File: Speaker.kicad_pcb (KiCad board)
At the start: 2 copper layers, 55.8 x 60 mm, 93 parts, among them J2 UJ20-C-H-G-SMT-1-P16-TR, SW1 SW_Push, SW2 Volume Up, SW3 Volume Down, SW4 Play/Pause, SW5 Power Switch, U2 MCP73871, U3 AP2112K-3.3, U4 MAX17048G_T10, U5 USBLC6-2SC6, U6 CH340X, U7 ESP32-WROOM-32, U8 MAX98357A, U9 USBLC6-2SC6

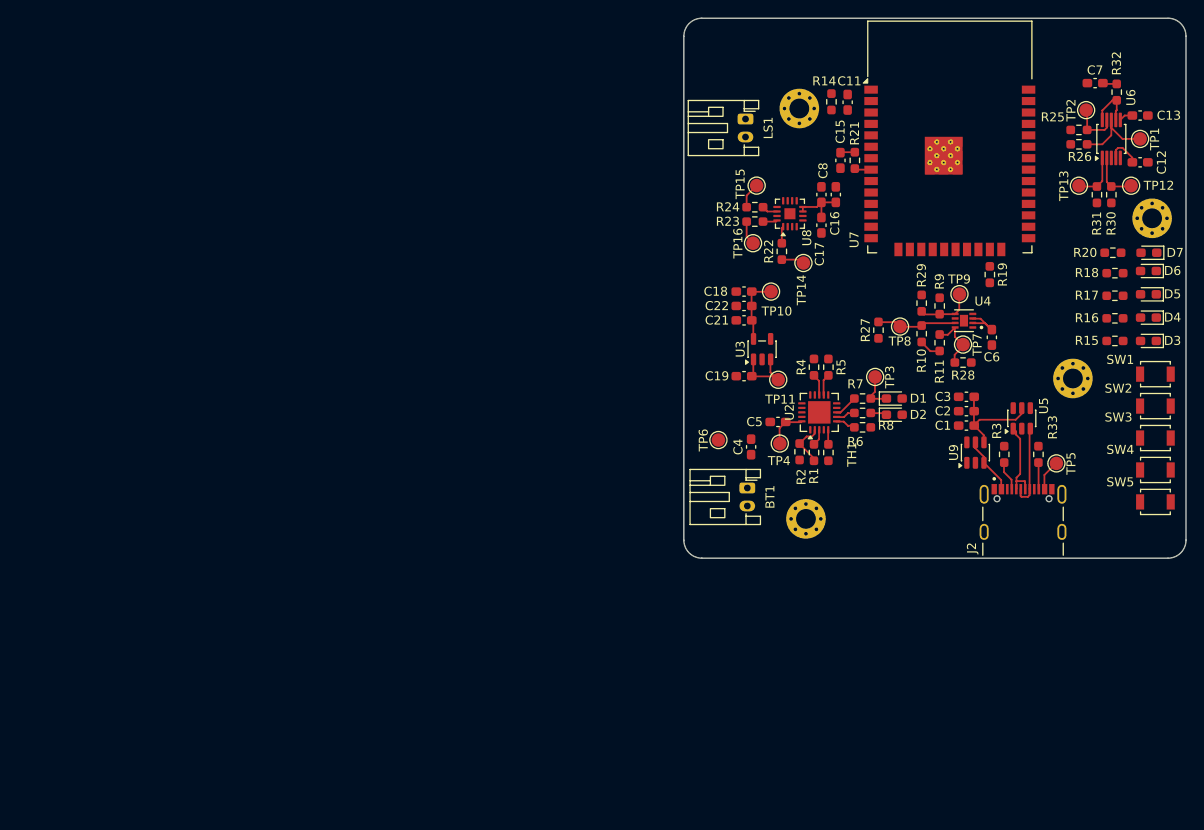
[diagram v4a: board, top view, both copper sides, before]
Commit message: Add 3d models and design rules
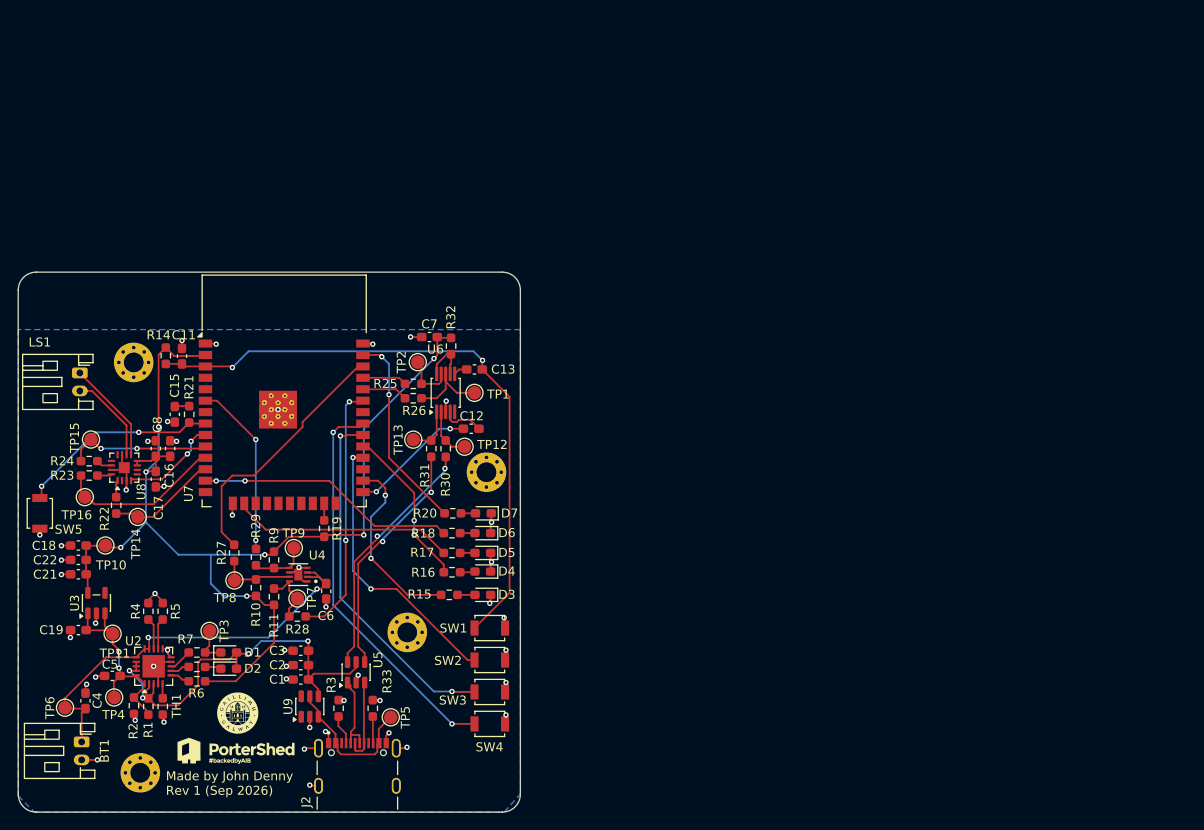
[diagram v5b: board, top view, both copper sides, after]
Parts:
- added G***: LOGO, LOGO, F.Cu at (157.0, 115.8)
- added G***: LOGO, LOGO, F.Cu at (157.2, 111.6)
- moved SW5 124.0 mm to (135.2, 89.4), turned to -90 degrees
- moved C12 80.0 mm to (183.2, 80.0), turned to 0 degrees
- moved TP12 79.5 mm to (182.4, 82.0)
- moved D6 79.5 mm to (184.5, 91.6)
- moved TP16 79.4 mm to (140.2, 87.6)
- moved D7 79.4 mm to (184.5, 89.4)
- moved TP2 79.4 mm to (177.2, 72.6)
- moved D5 79.4 mm to (184.5, 93.8)
- moved C18 79.2 mm to (139.5, 93.0)
- moved C19 79.2 mm to (139.5, 102.4)
- moved C21 79.2 mm to (139.5, 96.2)
- moved C22 79.2 mm to (139.5, 94.6)
- moved D3 79.2 mm to (184.5, 98.5)
- moved D4 79.2 mm to (184.5, 95.9)
- moved H4 79.2 mm to (184.9, 84.8)
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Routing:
- net VREG_3.3V: track 17.5 -> 124.0 mm, vias 0 -> 7
- net Net-(U7-EN): track 0.00 -> 69.2 mm, vias 0 -> 2
- net GND: track 0.00 -> 63.8 mm, vias 0 -> 47
- net Net-(U7-IO19): track 0.00 -> 44.1 mm, vias 0 -> 2
- net VBAT+: track 5.04 -> 47.5 mm, vias 0 -> 2
- net Net-(U7-IO18): track 0.00 -> 39.8 mm, vias 0 -> 2
- net VDD: track 13.8 -> 45.4 mm, vias 0 -> 4
- net Net-(U7-IO17): track 0.00 -> 31.3 mm, vias 0 -> 2
- net Net-(U7-IO14): track 0.00 -> 28.9 mm, vias 0 -> 2
- net FuelGaugeSDA: track 0.00 -> 28.6 mm, vias 0 -> 2
- net FuelGaugeSCL: track 0.00 -> 28.6 mm
- net D-: track 0.00 -> 27.5 mm, vias 0 -> 2
- net D+: track 0.00 -> 26.8 mm, vias 0 -> 2
- net Net-(U7-IO13): track 0.00 -> 24.8 mm
- net Net-(U7-IO23): track 0.00 -> 22.5 mm, vias 0 -> 2
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- added copper zone on B.Cu, net GND

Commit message: Update speaker PCB design
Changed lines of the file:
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@@
 		(start 140.308274 111.116726)
 		(end 138.133274 111.116726)
-		(width 0.2)
+		(width 0.4)
 		(layer "F.Cu")
 		(net 2)
@@
 		(start 138.033274 109.966783)
 		(end 138.033274 111.016726)
-		(width 0.2)
+		(width 0.4)
 		(layer "F.Cu")
 		(net 2)
@@
 		(start 139.883274 114.816726)
 		(end 139.883274 111.541726)
-		(width 0.2)
+		(width 0.4)
 		(layer "F.Cu")
 		(net 2)
@@
 		(start 145.945774 105.416726)
 		(end 142.583331 105.416726)
-		(width 0.2)
+		(width 0.4)
 		(layer "F.Cu")
 		(net 2)
@@
 		(start 142.583331 105.416726)
 		(end 138.033274 109.966783)
-		(width 0.2)
+		(width 0.4)
 		(layer "F.Cu")
 		(net 2)
@@
 		(start 146.883274 104.479226)
 		(end 145.945774 105.416726)
-		(width 0.2)
+		(width 0.4)
 		(layer "F.Cu")
 		(net 2)
@@
 		(start 146.883274 108.354226)
 		(end 145.945774 107.416726)
-		(width 0.2)
+		(width 0.4)
 		(layer "F.Cu")
 		(net 3)
@@
 		(start 143.468274 109.904226)
 		(end 143.468274 108.166726)
-		(width 0.2)
+		(width 0.4)
 		(layer "F.Cu")
 		(net 3)
@@
 		(start 143.468274 108.166726)
 		(end 144.130774 107.504226)
-		(width 0.2)
+		(width 0.4)
 		(layer "F.Cu")
 		(net 3)
@@
 		(start 145.820774 107.541726)
 		(end 144.218274 107.541726)
-		(width 0.2)
-		(layer "F.Cu")
-		(net 3)
+		(width 0.4)
+		(layer "F.Cu")
+		(net 3)

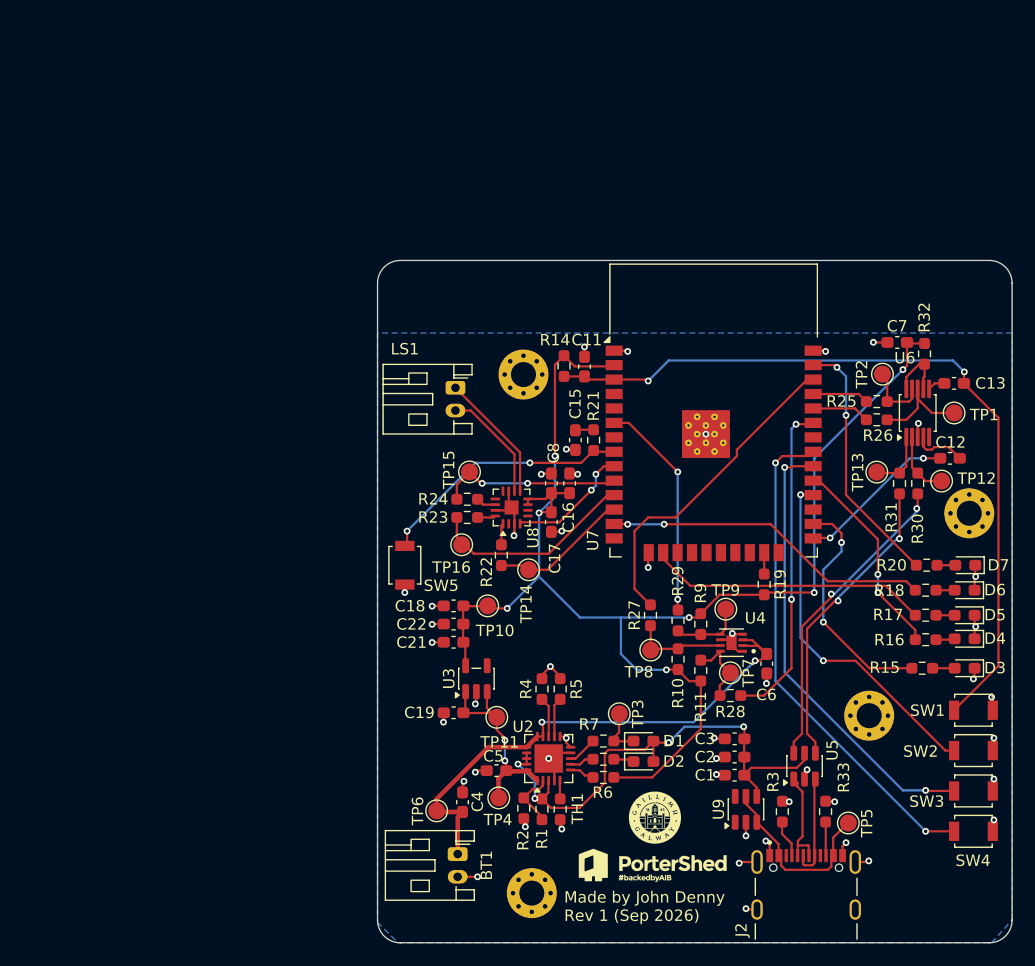
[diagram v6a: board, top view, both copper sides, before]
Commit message: Mostly finished schematic and pcb, getting codex to review it now
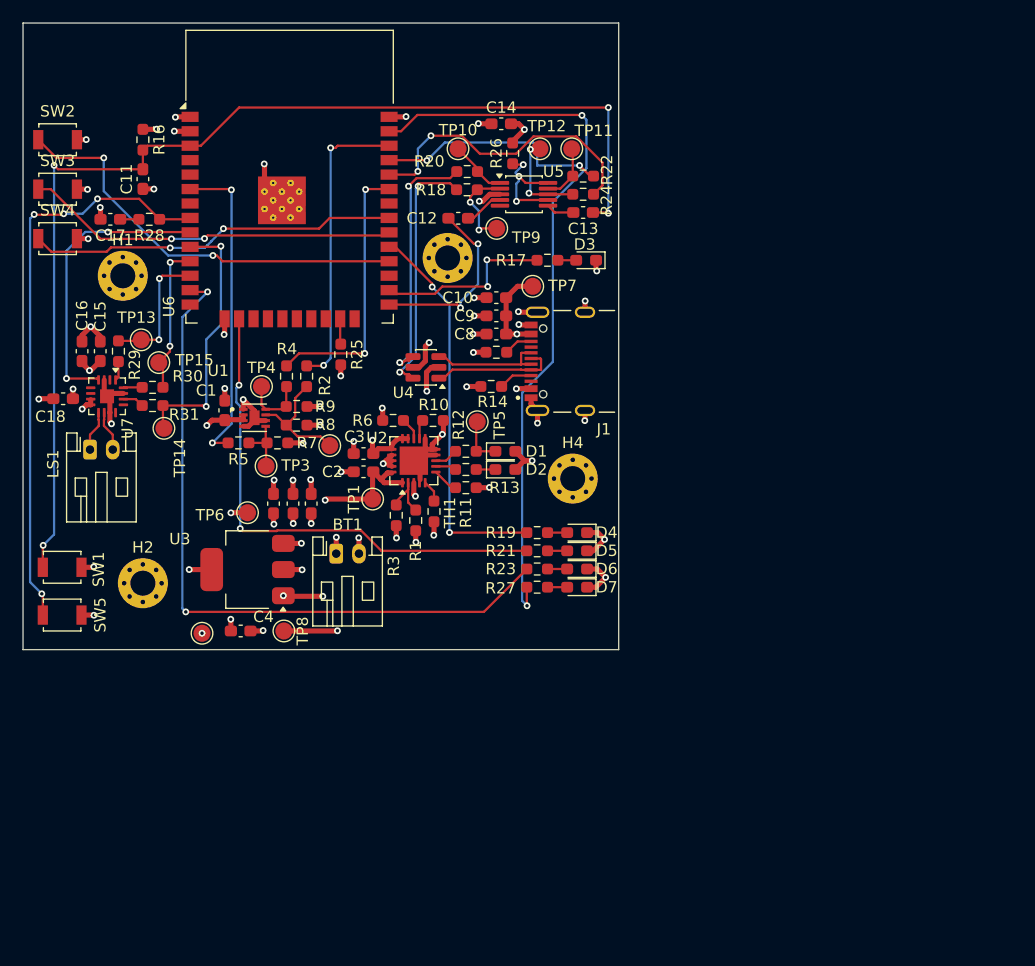
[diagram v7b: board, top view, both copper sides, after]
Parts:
- removed C19: 1uF, Capacitor_SMD:C_0603_1608Metric_Pad1.08x0.95mm_HandSolder
- removed C21: 100pF, Capacitor_SMD:C_0603_1608Metric_Pad1.08x0.95mm_HandSolder
- removed C22: 100nF, Capacitor_SMD:C_0603_1608Metric_Pad1.08x0.95mm_HandSolder
- removed G*** (x2): LOGO, LOGO
- removed H5, H6: MountingHole, MountingHole:MountingHole_2.2mm_M2_Pad_Via
- removed J2: UJ20-C-H-G-SMT-1-P16-TR, UJ20-C-H-G-SMT-1-P16-TR:SAMESKY_UJ20-C-H-G-SMT-1-P16-TR
- removed R32: 0, Resistor_SMD:R_0603_1608Metric_Pad0.98x0.95mm_HandSolder
- removed R33: 5.1k, Resistor_SMD:R_0603_1608Metric_Pad0.98x0.95mm_HandSolder
- removed TP16: TP_BCLK, TestPoint:TestPoint_Pad_D1.5mm
- removed U8: MAX98357A, Package_DFN_QFN:TQFN-16-1EP_3x3mm_P0.5mm_EP1.23x1.23mm
- removed U9: USBLC6-2SC6, Package_TO_SOT_SMD:SOT-23-6
- added C10: 1uF, Capacitor_SMD:C_0603_1608Metric_Pad1.08x0.95mm_HandSolder, F.Cu at (143.3, 65.9)
- added C14: 0.1uF, Capacitor_SMD:C_0603_1608Metric_Pad1.08x0.95mm_HandSolder, F.Cu at (143.7, 50.6)
- added C9: 100pF, Capacitor_SMD:C_0603_1608Metric_Pad1.08x0.95mm_HandSolder, F.Cu at (143.3, 67.5)
- added H1: MountingHole, MountingHole:MountingHole_2.2mm_M2_Pad_Via, F.Cu at (110.4, 64.0)
- added H2: MountingHole, MountingHole:MountingHole_2.2mm_M2_Pad_Via, F.Cu at (112.2, 91.0)
- added J1: UJ20-C-H-G-SMT-1-P16-TR, UJ20-C-H-G-SMT-1-P16-TR:SAMESKY_UJ20-C-H-G-SMT-1-P16-TR, F.Cu at (153.7, 71.5)
- added R12: ~, Resistor_SMD:R_0603_1608Metric_Pad0.98x0.95mm_HandSolder, F.Cu at (140.6, 79.4)
- added R13: ~, Resistor_SMD:R_0603_1608Metric_Pad0.98x0.95mm_HandSolder, F.Cu at (140.6, 81.0)
- added TP_VSYS_LDO1: TP_VSYS_LDO, TestPoint:TestPoint_Pad_D1.5mm, F.Cu at (117.4, 95.4)
- added U1: MAX17048G_T10, MAX17048G_T10:SON50P200X200X80-9N, F.Cu at (122.0, 76.5)
- C1: value 1uF -> 0.1uF
- C15: value 100nF -> 10uF
- C16: value 10uF -> 100nF
- C18: value 1uF -> 1nF
- C2: value 100pF -> 4.7uF
- C3: value 100nF -> 4.7uF
- C4: value 4.7uF -> 1uF
- C5: value 4.7uF -> 100nF
- C6: value 0.1uF -> 100pF
- C7: value 0.1uF -> 1uF
- C8: value 1nF -> 100nF
- R10: value 4.7k -> 10k
- R11: value 4.7k -> 470
- R14: value 10k -> 5.1k
- R15: value R -> 5.1k
- R16: value R -> 10k
- R18, R20: value R -> 0
- R19, R21: value 10k -> R
- R2: value 110k -> 0
- R23, R27: value 0 -> R
- R25, R28: value 0 -> 10k
- R3: value 5.1k -> 110k
- R4: value 1k -> 0
- R5: value 10k -> 0
- R6: value 470 -> 1k
- R7, R8: value ~ -> 4.7k
- TP1: value TP_UART_TX -> TP_VSYS
- TP10: value TP_VREG3.3 -> TP_D+
- TP11: value TP_VSYS_LDO -> TP_UART_RX
- TP12: value TP_D- -> TP_UART_TX
- TP13: value TP_D+ -> TP_DIN
- TP15: value TP_DIN -> TP_BCLK
- TP2: value TP_UART_RX -> TP_FG_SCL
- TP3: value TP_Charging -> TP_FG_ALRT
- TP4: value TP_VSYS -> TP_FG_SDA
- TP5: value TP_VDD -> TP_Charging
- TP6: value TP_VBAT+ -> TP_VREG3.3
- TP7: value TP_FG_SDA -> TP_VDD
- TP8: value TP_FG_SCL -> TP_VBAT+
- TP9: value TP_FG_ALRT -> TP_D-
- U3: value AP2112K-3.3 -> LT1963AxST-3.3; footprint Package_TO_SOT_SMD:SOT-23-5 -> Package_TO_SOT_SMD:SOT-223-3_TabPin2
- U4: value MAX17048G_T10 -> USBLC6-2SC6; footprint MAX17048G_T10:SON50P200X200X80-9N -> Package_TO_SOT_SMD:SOT-23-6
- U5: value USBLC6-2SC6 -> CH340X; footprint Package_TO_SOT_SMD:SOT-23-6 -> Package_SO:MSOP-10_3x3mm_P0.5mm
- U6: value CH340X -> ESP32-WROOM-32; footprint Package_SO:MSOP-10_3x3mm_P0.5mm -> RF_Module:ESP32-WROOM-32
- U7: value ESP32-WROOM-32 -> MAX98357A; footprint RF_Module:ESP32-WROOM-32 -> Package_DFN_QFN:TQFN-16-1EP_3x3mm_P0.5mm_EP1.23x1.23mm
- moved SW2 96.8 mm to (104.7, 52.0)
- moved SW3 96.4 mm to (104.7, 56.4)
- moved SW4 95.9 mm to (104.7, 60.7)
- moved R16 81.7 mm to (112.2, 52.0), turned to -90 degrees
- moved SW1 81.1 mm to (105.1, 89.6)
- moved R30 67.8 mm to (113.0, 73.8), turned to 180 degrees
- moved R28 66.1 mm to (112.8, 59.0)
- moved R31 66.0 mm to (113.0, 75.4), turned to 180 degrees
- moved TP13 65.7 mm to (112.0, 69.6), turned to -90 degrees
- moved U6 58.0 mm to (125.1, 58.2), turned to 0 degrees
- moved C7 56.6 mm to (123.7, 84.0), turned to -90 degrees
- moved U5 56.0 mm to (145.7, 56.8), turned to 0 degrees
- moved C1 55.1 mm to (119.4, 75.8), turned to 90 degrees
- moved H3 54.7 mm to (139.0, 62.4)
- moved R29 54.6 mm to (110.0, 70.6), turned to -90 degrees
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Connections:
- C1 pad 1: GND -> VBAT+
- C1 pad 2: VDD -> GND
- C11 pad 2: Net-(U7-EN) -> Enable
- C12 pad 1: Net-(U7-IO0) -> Net-(U6-IO0)
- C12 pad 2: Net-(U6-~{RTS}) -> Net-(U5-~{RTS})
- C13 pad 1: Net-(U7-EN) -> Enable
- C13 pad 2: Net-(U6-TNOW/~{DTR}) -> Net-(U5-TNOW/~{DTR})
- C15 pad 1: Net-(C15-Pad1) -> GND
- C15 pad 2: GND -> VREG_3.3V
- C17 pad 1: GND -> Net-(C17-Pad1)
- C17 pad 2: VREG_3.3V -> GND
- C2 pad 1: GND -> VSYS
- C2 pad 2: VDD -> GND
- C3 pad 1: GND -> VBAT+
- C3 pad 2: VDD -> GND
- C4 pad 1: VBAT+ -> GND
- C4 pad 2: GND -> VSYS
- C5 pad 1: VSYS -> GND
- C5 pad 2: GND -> VREG_3.3V
- C6 pad 1: VBAT+ -> GND
- C6 pad 2: GND -> VREG_3.3V
- C8 pad 2: VREG_3.3V -> VDD
- LS1 pad 1: Net-(U8-OUTP) -> /MCU/Speaker+
- LS1 pad 2: Net-(U8-OUTN) -> /MCU/Speaker-
- R10 pad 1: Net-(U4-SCL) -> GND
- R10 pad 2: VREG_3.3V -> Net-(U2-PROG3)
- R11 pad 1: Net-(U4-SDA) -> Net-(U2-~{PG})
- R14 pad 1: VREG_3.3V -> GND
- R14 pad 2: Net-(U7-EN) -> Net-(J1-CC1)
- R15 pad 1: Net-(U7-IO4) -> Net-(J1-CC2)
- R15 pad 2: Net-(D3-A) -> GND
- R16 pad 1: Net-(U7-IO5) -> VREG_3.3V
- R16 pad 2: Net-(D4-A) -> Enable
- R17 pad 1: Net-(U7-IO13) -> Net-(U6-IO4)
- R17 pad 2: Net-(D5-A) -> Net-(D3-A)
- R18 pad 1: Net-(U7-IO14) -> Net-(U5-UD-)
- R18 pad 2: Net-(D6-A) -> D-
- R19 pad 1: Net-(U7-IO15) -> Net-(U6-IO5)
- R19 pad 2: VREG_3.3V -> Net-(D4-A)
- R2 pad 1: GND -> FuelGaugeSCL
- R2 pad 2: Net-(U2-VPCC) -> Net-(U1-SCL)
- R20 pad 1: Net-(U7-IO23) -> Net-(U5-UD+)
- R20 pad 2: Net-(D7-A) -> D+
- R21 pad 1: Net-(U7-IO32) -> Net-(U6-IO13)
- R21 pad 2: Net-(C15-Pad1) -> Net-(D5-A)
- R22 pad 1: /MCU/AMP_DIN -> /MCU/RX_UART
- R22 pad 2: Net-(U8-DIN) -> Net-(U5-RXD)
- R23 pad 1: /MCU/AMP_BCLK -> Net-(U6-IO14)
- R23 pad 2: Net-(U8-BCLK) -> Net-(D6-A)
- R24 pad 1: /MCU/AMP_LRCLK -> /MCU/TX_UART
- R24 pad 2: Net-(U8-LRCLK) -> Net-(U5-TXD)
- R25 pad 1: /MCU/RX_UART -> Net-(U6-IO15)
- R25 pad 2: Net-(U6-RXD) -> VREG_3.3V
- R26 pad 1: /MCU/TX_UART -> Net-(U5-V3)
- R26 pad 2: Net-(U6-TXD) -> VREG_3.3V
- R27 pad 1: FuelGaugeSCL -> Net-(U6-IO23)
- R27 pad 2: Net-(U4-SCL) -> Net-(D7-A)
- R28 pad 1: FuelGaugeSDA -> Net-(U6-IO32)
- R28 pad 2: Net-(U4-SDA) -> Net-(C17-Pad1)
- R29 pad 1: Net-(U4-~{ALERT}) -> /MCU/AMP_DIN
- R29 pad 2: FuelGaugeAlert -> Net-(U7-DIN)
- R3 pad 2: Net-(J2-CC1) -> Net-(U2-VPCC)
- R30 pad 1: Net-(U6-UD-) -> /MCU/AMP_BCLK
- R30 pad 2: D- -> Net-(U7-BCLK)
- R31 pad 1: Net-(U6-UD+) -> /MCU/AMP_LRCLK
- R31 pad 2: D+ -> Net-(U7-LRCLK)
- R4 pad 1: GND -> FuelGaugeSDA
- R4 pad 2: Net-(U2-PROG1) -> Net-(U1-SDA)
- R5 pad 1: GND -> Net-(U1-~{ALERT})
- R5 pad 2: Net-(U2-PROG3) -> FuelGaugeAlert
- R6 pad 1: Net-(U2-~{PG}) -> GND
- R6 pad 2: VREG_3.3V -> Net-(U2-PROG1)
- R7 pad 1: Net-(U2-STAT1/~{LBO}) -> Net-(U1-~{ALERT})
- R7 pad 2: Net-(D1-K) -> VREG_3.3V
- R8 pad 1: Net-(U2-STAT2) -> Net-(U1-SCL)
- R8 pad 2: Net-(D2-K) -> VREG_3.3V
- R9 pad 1: Net-(U4-~{ALERT}) -> Net-(U1-SDA)
- SW1 pad 2: Net-(U7-EN) -> Enable
- SW2 pad 1: Net-(U7-IO17) -> Net-(U6-IO17)
- SW3 pad 1: Net-(U7-IO18) -> Net-(U6-IO18)
- SW4 pad 1: Net-(U7-IO19) -> Net-(U6-IO19)
- SW5 pad 1: Net-(U7-IO32) -> Net-(U6-IO32)
- TP1 pad 1: Net-(U6-TXD) -> VSYS
- TP10 pad 1: VREG_3.3V -> Net-(U5-UD+)
- TP11 pad 1: VSYS -> Net-(U5-RXD)
- TP12 pad 1: Net-(U6-UD-) -> Net-(U5-TXD)
- TP13 pad 1: Net-(U6-UD+) -> /MCU/AMP_DIN
- TP14 pad 1: /MCU/AMP_DIN -> /MCU/AMP_LRCLK
- TP15 pad 1: /MCU/AMP_LRCLK -> /MCU/AMP_BCLK
- TP2 pad 1: Net-(U6-RXD) -> Net-(U1-SCL)
- TP3 pad 1: Net-(D1-K) -> Net-(U1-~{ALERT})
- TP4 pad 1: VSYS -> Net-(U1-SDA)
- TP5 pad 1: Net-(U9-VBUS) -> Net-(D1-K)
- TP6 pad 1: VBAT+ -> VREG_3.3V
- TP7 pad 1: Net-(U4-SDA) -> VDD
- TP8 pad 1: Net-(U4-SCL) -> VBAT+
- TP9 pad 1: Net-(U4-~{ALERT}) -> Net-(U5-UD-)
- U3 pad 3: VSYS -> VREG_3.3V
- U4 pad 1: GND -> /Power/USBtoSchottky-
- U4 pad 2: VBAT+ -> GND
- U4 pad 3: VBAT+ -> /Power/USBtoSchottky+
- U4 pad 4: GND -> D+
- U4 pad 5: Net-(U4-~{ALERT}) -> VDD
- U4 pad 6: GND -> D-
- U5 pad 1: Net-(J2-D2_N) -> Net-(U5-UD+)
- U5 pad 2: GND -> Net-(U5-UD-)
- U5 pad 3: Net-(J2-D2_P) -> GND
- U5 pad 4: D+ -> Net-(U5-~{RTS})
- U5 pad 5: VDD -> unconnected-(U5-~{CTS}-Pad5)
- U5 pad 6: D- -> Net-(U5-TNOW/~{DTR})
- U6 pad 1: Net-(U6-UD+) -> GND
- U6 pad 10: Net-(U6-V3) -> /MCU/AMP_LRCLK
- U6 pad 2: Net-(U6-UD-) -> VREG_3.3V
- U6 pad 3: GND -> Enable
- U6 pad 4: Net-(U6-~{RTS}) -> unconnected-(U6-SENSOR_VP-Pad4)
- U6 pad 6: Net-(U6-TNOW/~{DTR}) -> FuelGaugeAlert
- U6 pad 7: Net-(U6-V3) -> unconnected-(U6-IO35-Pad7)
- U6 pad 8: Net-(U6-TXD) -> Net-(U6-IO32)
- U6 pad 9: Net-(U6-RXD) -> /MCU/AMP_SDM
- U7 pad 1: GND -> Net-(U7-DIN)
- U7 pad 10: /MCU/AMP_LRCLK -> /MCU/Speaker-
- U7 pad 11: /MCU/AMP_BCLK -> GND
- U7 pad 12: /MCU/AMP_DIN -> unconnected-(U7-NC-Pad12)
- U7 pad 13: Net-(U7-IO14) -> unconnected-(U7-NC-Pad13)
- U7 pad 14: unconnected-(U7-IO12-Pad14) -> Net-(U7-LRCLK)
- U7 pad 16: Net-(U7-IO13) -> Net-(U7-BCLK)
- U7 pad 17: unconnected-(U7-SHD/SD2-Pad17) -> GND
- U7 pad 2: VREG_3.3V -> unconnected-(U7-GAIN_SLOT-Pad2)
- U7 pad 3: Net-(U7-EN) -> GND
- U7 pad 4: unconnected-(U7-SENSOR_VP-Pad4) -> /MCU/AMP_SDM
- U7 pad 6: FuelGaugeAlert -> unconnected-(U7-NC-Pad6)
- U7 pad 7: unconnected-(U7-IO35-Pad7) -> VREG_3.3V
- U7 pad 8: Net-(U7-IO32) -> VREG_3.3V
- U7 pad 9: /MCU/AMP_SDM -> /MCU/Speaker+
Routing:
- net VREG_3.3V: track 124.0 -> 21.9 mm, vias 7 -> 16
- net Enable: track 0.00 -> 98.6 mm, vias 0 -> 4
- net Net-(U7-EN): track 69.2 -> 0.00 mm, vias 2 -> 0
- net Net-(U6-IO23): track 0.00 -> 65.0 mm, vias 0 -> 2
- net Net-(U6-IO14): track 0.00 -> 62.3 mm, vias 0 -> 2
- net Net-(U6-IO32): track 0.00 -> 50.9 mm, vias 0 -> 4
- net Net-(U6-IO13): track 0.00 -> 44.7 mm, vias 0 -> 2
- net Net-(U7-IO19): track 44.1 -> 0.00 mm, vias 2 -> 0
- net Net-(U7-IO18): track 39.8 -> 0.00 mm, vias 2 -> 0
- net Net-(U6-IO17): track 0.00 -> 37.0 mm, vias 0 -> 2
- net Net-(U6-IO5): track 0.00 -> 34.4 mm, vias 0 -> 2
- net Net-(U6-IO18): track 0.00 -> 32.9 mm, vias 0 -> 2
- net Net-(U6-IO19): track 0.00 -> 32.6 mm, vias 0 -> 2
- net Net-(U7-IO17): track 31.3 -> 0.00 mm, vias 2 -> 0
- net Net-(U7-IO14): track 28.9 -> 0.00 mm, vias 2 -> 0
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- added copper zone on In2.Cu, net GND
- added copper zone on In1.Cu, net VREG_3.3V
- removed copper zone on B.Cu, net GND
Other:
- board size 55.8 x 60 mm -> 52.4 x 55.1 mm
- copper layers 2 -> 4
- board text removed: "Made by John Denny Rev 1 (Sep 2026)"
